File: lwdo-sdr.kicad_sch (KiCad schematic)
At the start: 21 parts, among them J101 IN1, J102 IN2, J103 IN3, J104 IN4, J105 USB_B, J106 CLK_OUT, J107 REF_IN

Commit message: Schematic update
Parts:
- R101, R102, R103, R104, R105, R106, R107, R108, R109, R110, R111: value 240 -> 220

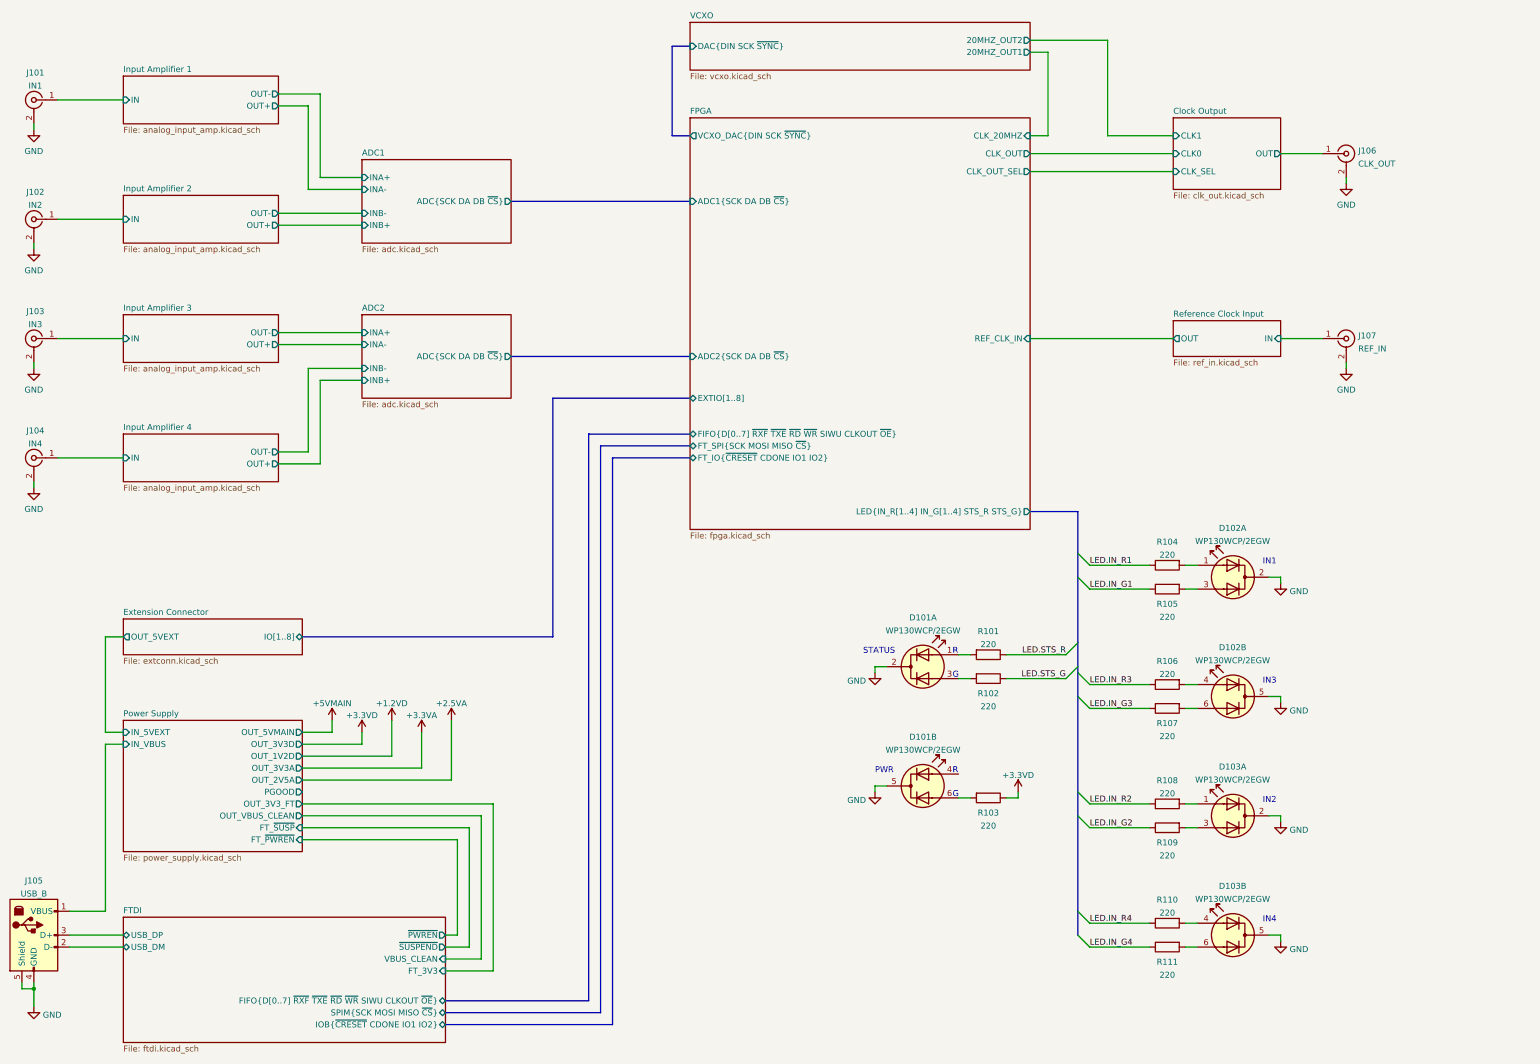
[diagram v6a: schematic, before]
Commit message: Schematic: better LDO output capacitor selection, clarified BOM
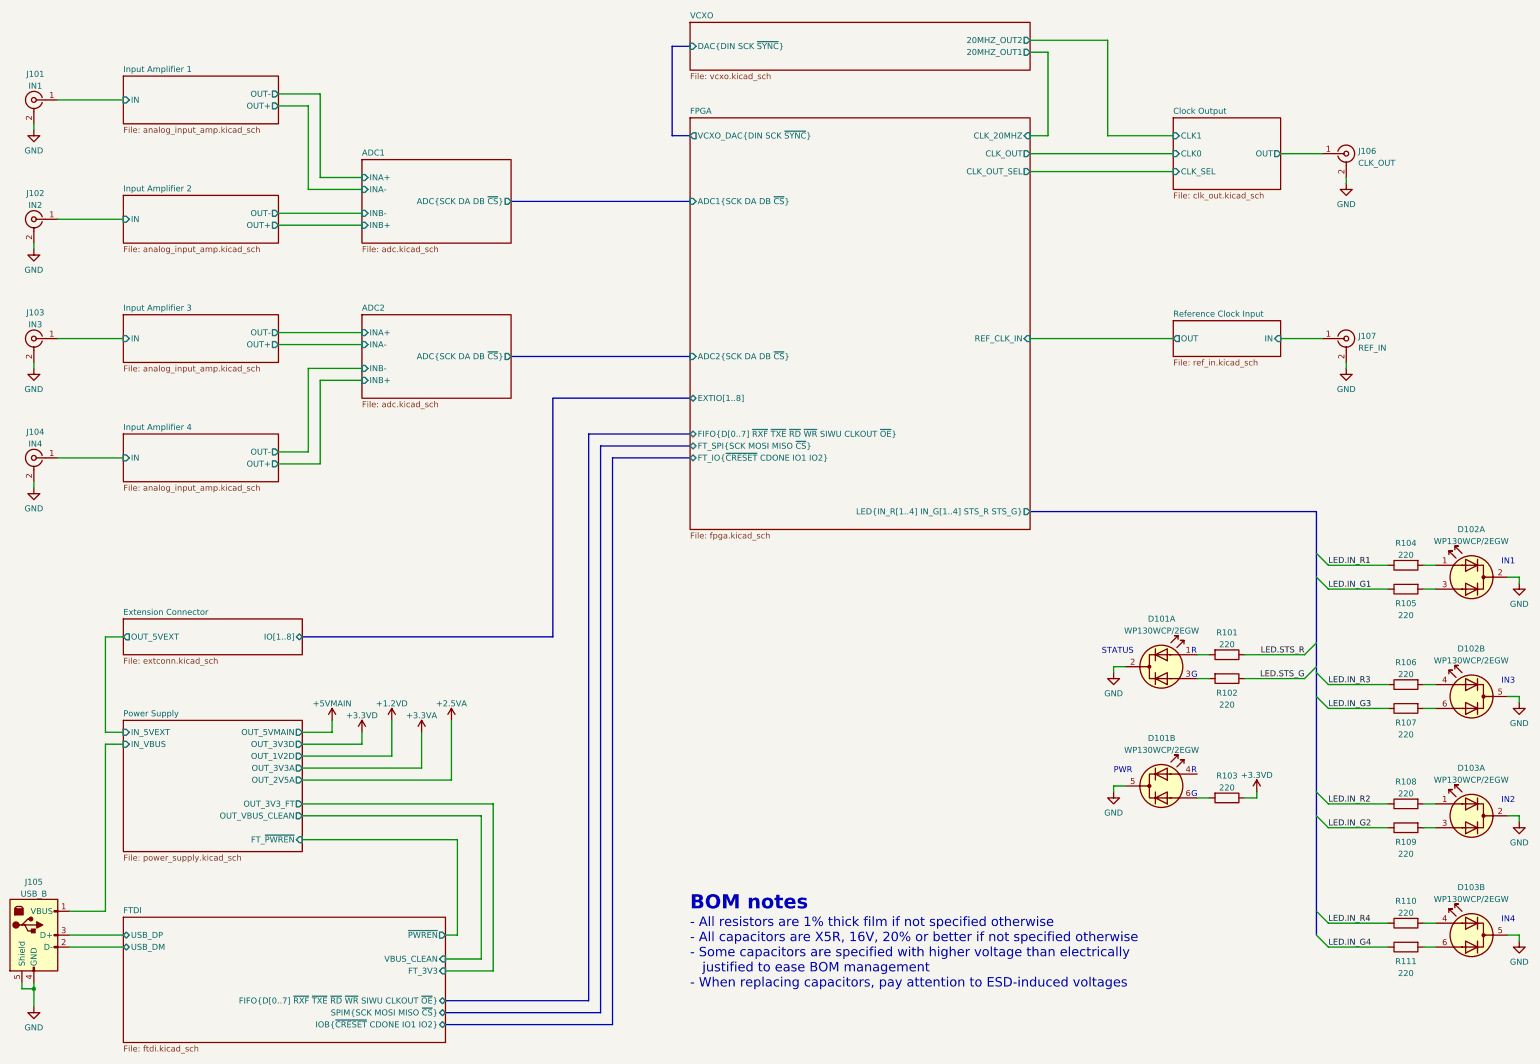
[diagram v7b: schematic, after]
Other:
- sheet FTDI ports: added none; removed ~{SUSPEND}
- sheet Power Supply ports: added none; removed FT_~{SUSP}, PGOOD
- note added: "- All resistors are 1% thick film if not specified otherwise - All capacitors are X5R, 16V, 20% or better if not specified otherwise - Some capacitors are specified with higher voltage than electrically justified to ease BOM management - When replacing capacitors, pay attention to ESD-induced voltages"
- note added: "BOM notes"
- moved on the sheet: D101A, D101B, D102A, D102B, D103A, D103B, R101, R102, R103, R104, R105, R106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

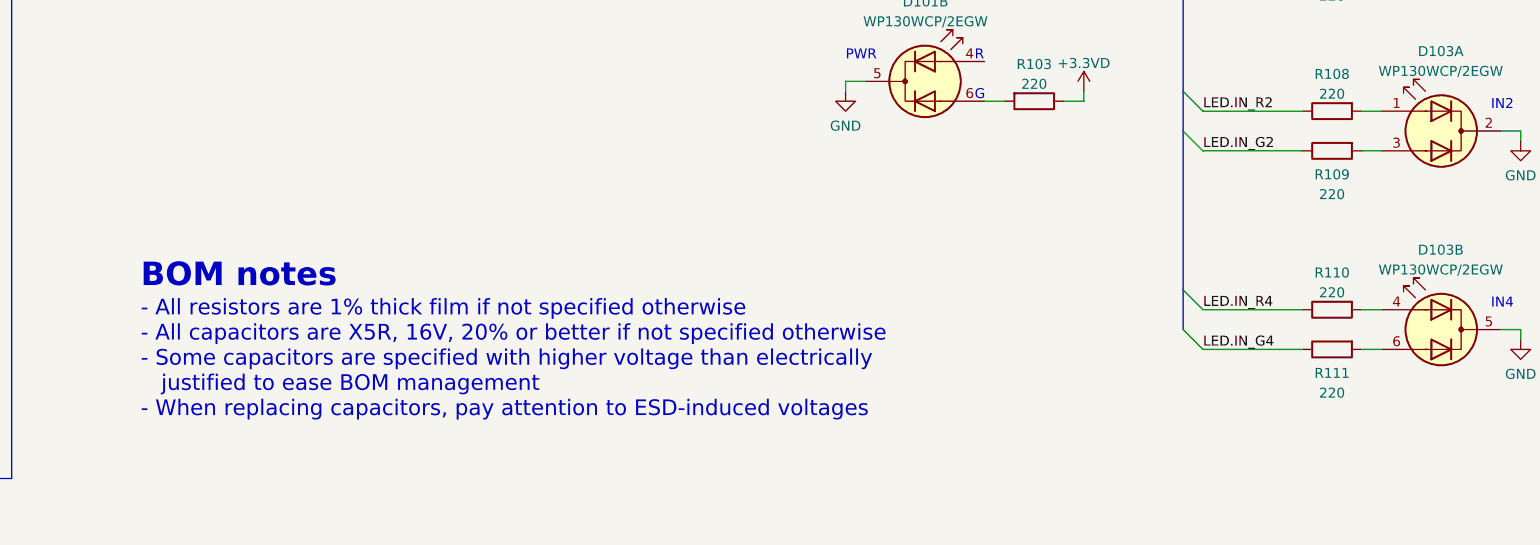
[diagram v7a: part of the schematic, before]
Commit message: Schematic: yet another update -Improve way caps are specified once again -Update cap voltages based on ESD simulation -Make anti-aliasing LC filter more practical - with much less inductors -Specify Mfr & MfrPN for almost all components (most from Mouser, some from Digikey)
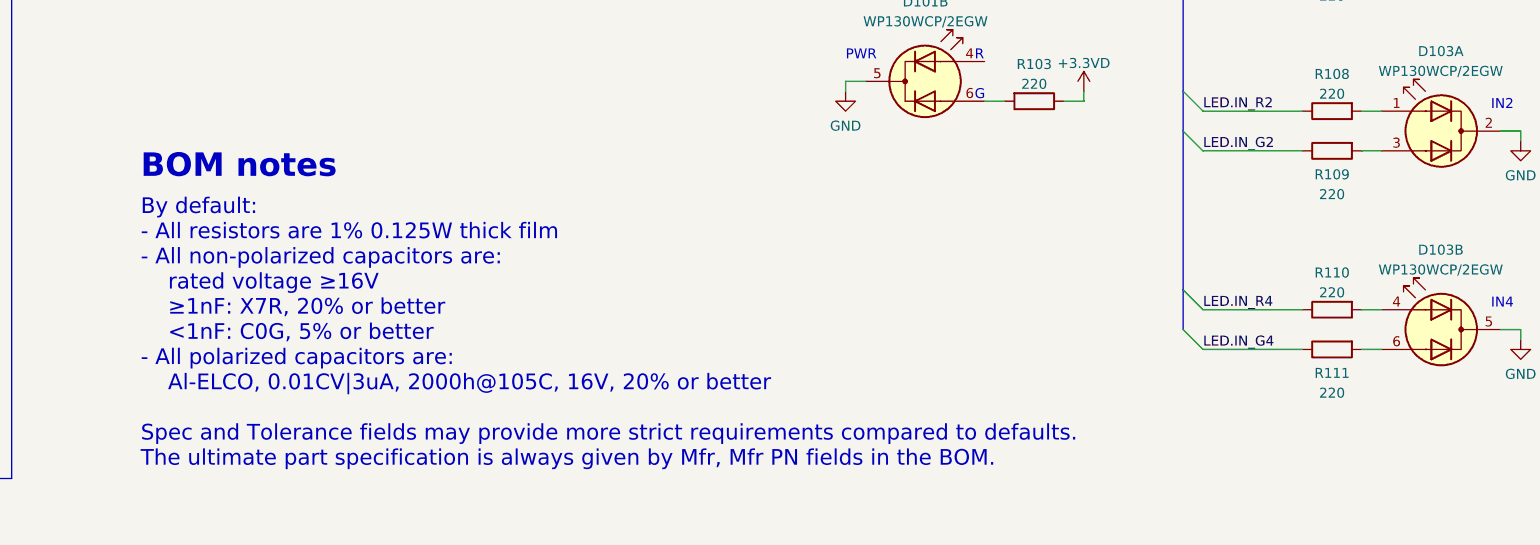
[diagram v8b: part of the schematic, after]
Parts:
- D101, D102, D103: Mfr (none) -> Kingbright; Mfr PN (none) -> WP130WCP/2EGW
- J105: Mfr (none) -> Amphenol; Mfr PN (none) -> 61729-1011BLF
- R101, R102, R103, R104, R105, R106, R107, R108, R109, R110, R111: Tolerance 5% -> (none)
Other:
- note added: "By default: - All resistors are 1% 0.125W thick film - All non-polarized capacitors are: rated voltage ≥16V ≥1nF: X7R, 20% or better <1nF: C0G, 5% or better - All polarized capacitors are: Al-ELCO, 0.01CV|3uA, 2000h@105C, 16V, 20% or better Spec and Tolerance fields may provide more strict requirements compared to defaults. The ultimate part specification is always given by Mfr, Mfr PN fields in 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"
- note removed: "- All resistors are 1% thick film if not specified otherwise - All capacitors are X5R, 16V, 20% or better if not specified otherwise - Some capacitors are specified with higher voltage than electrically justified to ease BOM management - When replacing capacitors, pay attention to ESD-induced voltages"
